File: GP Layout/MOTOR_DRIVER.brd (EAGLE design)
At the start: 91.4 x 97.5 mm, 34 parts, among them U2 CSD18502KCS_KCS_3, U3 MIC4604YM, U4 CSD18502KCS_KCS_3, U5 CSD18502KCS_KCS_3, U6 MIC4604YM, U7 ATMEGA328P_TQFP, Y1 16MHz

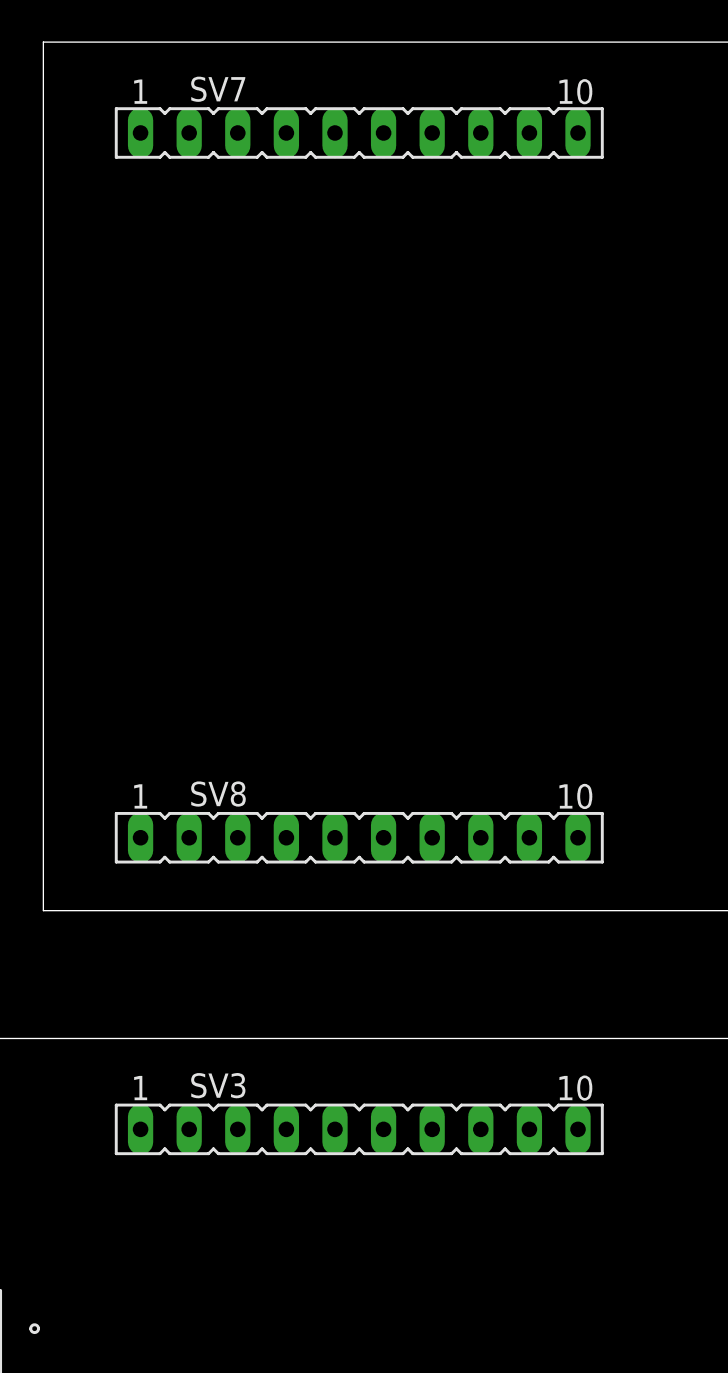
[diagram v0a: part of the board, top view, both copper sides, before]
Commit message: component placement
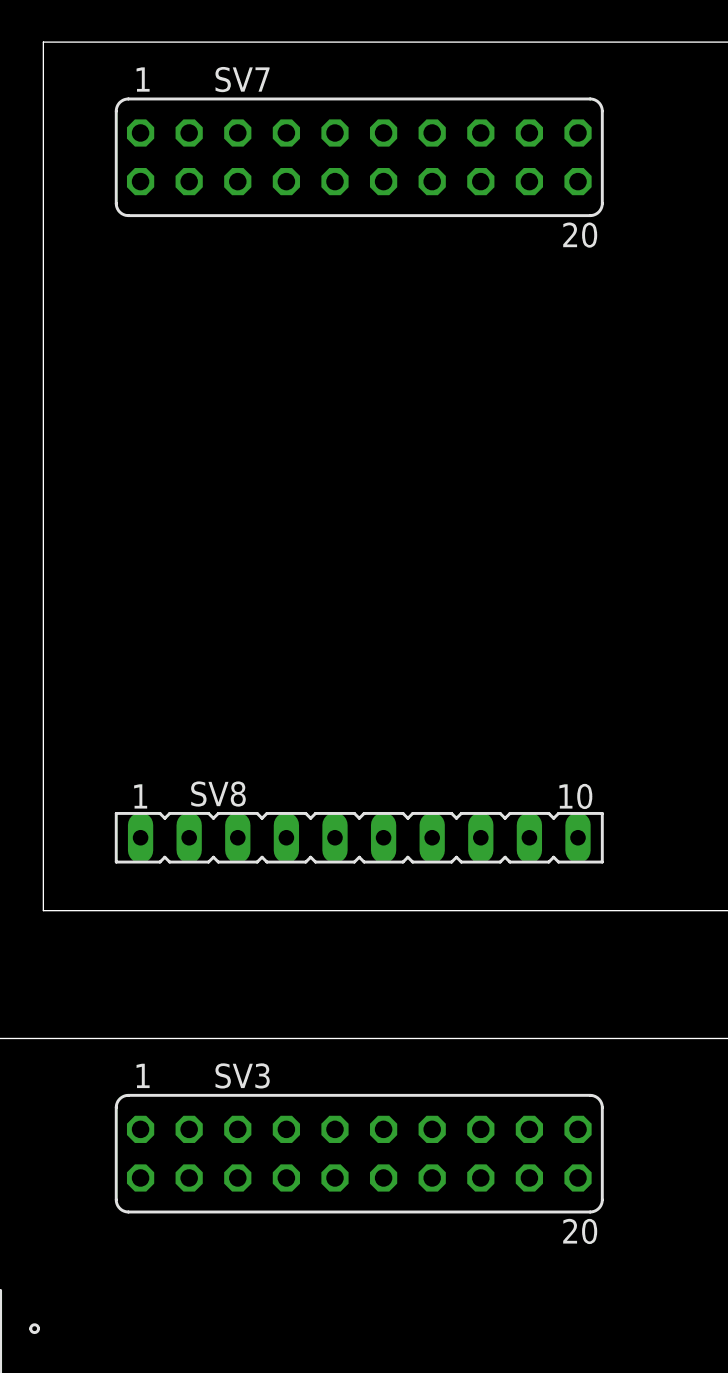
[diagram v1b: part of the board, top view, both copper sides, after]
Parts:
- SV3, SV7: device con-lsta:FE10 -> con-lsta:FE10-2
- moved SV3 1.27 mm to (69.8, 39.4)
- moved SV7 1.27 mm to (69.8, 91.4)
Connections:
- new net N$27: SV3.12
- net 3_3V: now also SV3.9
- net 5V: now also SV3.18, SV3.7
- net BLT_RX: now also SV3.1
- net BLT_TX: now also SV3.3
- net CAMERA_A0: now also SV3.17
- net CAMERA_CLK: now also SV3.13
- net CAMERA_SI: now also SV3.15
- net GND: now also SV3.11, SV3.14, SV3.5
- net HALL: now also SV3.16
- net RX: now also SV3.20
- net TX: now also SV3.19
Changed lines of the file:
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@@
 <attribute name="MF" value="" x="21.59" y="3.81" size="1.778" layer="27" display="off"/>
-</element>
-<element name="SV3" library="con-lsta" package="FE10" value="" x="69.85" y="40.64">
-<attribute name="OC_FARNELL" value="unknown" x="69.85" y="40.64" size="1.778" layer="27" display="off"/>
-<attribute name="MPN" value="" x="69.85" y="40.64" size="1.778" layer="27" display="off"/>
-<attribute name="OC_NEWARK" value="unknown" x="69.85" y="40.64" size="1.778" layer="27" display="off"/>
-<attribute name="MF" value="" x="69.85" y="40.64" size="1.778" layer="27" display="off"/>
 </element>
 <element name="SV4" library="con-lsta" package="FE10" value="" x="69.85" y="3.81">
@@
 <attribute name="MF" value="" x="21.59" y="55.88" size="1.778" layer="27" display="off"/>
 </element>
-<element name="SV7" library="con-lsta" package="FE10" value="" x="69.85" y="92.71">
-<attribute name="OC_FARNELL" value="unknown" x="69.85" y="92.71" size="1.778" layer="27" display="off"/>
-<attribute name="MPN" value="" x="69.85" y="92.71" size="1.778" layer="27" display="off"/>
-<attribute name="OC_NEWARK" value="unknown" x="69.85" y="92.71" size="1.778" layer="27" display="off"/>
-<attribute name="MF" value="" x="69.85" y="92.71" size="1.778" layer="27" display="off"/>
-</element>
 <element name="SV8" library="con-lsta" package="FE10" value="" x="69.85" y="55.88">
 <attribute name="OC_FARNELL" value="unknown" x="69.85" y="55.88" size="1.778" layer="27" display="off"/>
@@
 <attribute name="OC_NEWARK" value="unknown" x="69.85" y="55.88" size="1.778" layer="27" display="off"/>
 <attribute name="MF" value="" x="69.85" y="55.88" size="1.778" layer="27" display="off"/>
+</element>
+<element name="SV3" library="con-lsta" package="FE10-2" value="" x="69.85" y="39.37">
+<attribute name="OC_FARNELL" value="unknown" x="69.85" y="39.37" size="1.778" layer="27" display="off"/>
+<attribute name="MPN" value="" x="69.85" y="39.37" size="1.778" layer="27" display="off"/>
+<attribute name="OC_NEWARK" value="unknown" x="69.85" y="39.37" size="1.778" layer="27" display="off"/>
+<attribute name="MF" value="" x="69.85" y="39.37" size="1.778" layer="27" display="off"/>
+</element>
+<element name="SV7" library="con-lsta" package="FE10-2" value="" x="69.85" y="91.44">
+<attribute name="OC_FARNELL" value="unknown" x="69.85" y="91.44" size="1.778" layer="27" display="off"/>
+<attribute name="MPN" value="" x="69.85" y="91.44" size="1.778" layer="27" display="off"/>
+<attribute name="OC_NEWARK" value="unknown" x="69.85" y="91.44" size="1.778" layer="27" display="off"/>
+<attribute name="MF" value="" x="69.85" y="91.44" size="1.778" layer="27" display="off"/>
 </element>
 </elements>
@@
 <contactref element="S1" pad="12"/>
 <contactref element="SV1" pad="10"/>
-<wire x1="79.3242" y1="17.78" x2="79.3242" y2="20.32" width="0" layer="19" extent="1-1"/>
+<contactref element="SV3" pad="5"/>
+<contactref element="SV3" pad="11"/>
+<contactref element="SV3" pad="14"/>
+<wire x1="73.66" y1="38.1" x2="71.12" y2="40.64" width="0" layer="19" extent="1-1"/>
+<wire x1="63.5" y1="40.64" x2="71.12" y2="40.64" width="0" layer="19" extent="1-1"/>
+<wire x1="48.26" y1="34.29" x2="63.5" y2="40.64" width="0" layer="19" extent="1-1"/>
+<wire x1="48.26" y1="30.226" x2="48.26" y2="34.29" width="0" layer="19" extent="1-1"/>
+<wire x1="45.72" y1="24.13" x2="48.26" y2="30.226" width="0" layer="19" extent="1-1"/>
+<wire x1="53.34" y1="21.59" x2="45.72" y2="24.13" width="0" layer="19" extent="1-1"/>
+<wire x1="59.2074" y1="17.71" x2="53.34" y2="21.59" width="0" layer="19" extent="1-1"/>
+<wire x1="59.2074" y1="16.11" x2="59.2074" y2="17.71" width="0" layer="19" extent="1-1"/>
+<wire x1="67.7926" y1="16.91" x2="59.2074" y2="17.71" width="0" layer="19" extent="1-1"/>
+<wire x1="50.8" y1="11.43" x2="59.2074" y2="16.11" width="0" layer="19" extent="1-1"/>
+<wire x1="79.3242" y1="17.78" x2="67.7926" y2="16.91" width="0" layer="19" extent="1-1"/>
+<wire x1="79.3242" y1="20.32" x2="79.3242" y2="17.78" width="0" layer="19" extent="1-1"/>
 <wire x1="79.3242" y1="15.24" x2="79.3242" y2="17.78" width="0" layer="19" extent="1-1"/>
 <wire x1="79.3242" y1="12.7" x2="79.3242" y2="15.24" width="0" layer="19" extent="1-1"/>
 <wire x1="79.3242" y1="10.16" x2="79.3242" y2="12.7" width="0" layer="19" extent="1-1"/>
-<wire x1="67.7926" y1="16.91" x2="79.3242" y2="17.78" width="0" layer="19" extent="1-1"/>
-<wire x1="59.2074" y1="16.11" x2="67.7926" y2="16.91" width="0" layer="19" extent="1-1"/>
-<wire x1="59.2074" y1="17.71" x2="59.2074" y2="16.11" width="0" layer="19" extent="1-1"/>
-<wire x1="53.34" y1="21.59" x2="59.2074" y2="17.71" width="0" layer="19" extent="1-1"/>
-<wire x1="45.72" y1="24.13" x2="53.34" y2="21.59" width="0" layer="19" extent="1-1"/>
-<wire x1="48.26" y1="30.226" x2="45.72" y2="24.13" width="0" layer="19" extent="1-1"/>
-<wire x1="48.26" y1="34.29" x2="48.26" y2="30.226" width="0" layer="19" extent="1-1"/>
-<wire x1="50.8" y1="11.43" x2="59.2074" y2="16.11" width="0" layer="19" extent="1-1"/>
 <wire x1="33.02" y1="40.64" x2="48.26" y2="34.29" width="0" layer="19" extent="1-1"/>
 <wire x1="12.7" y1="24.13" x2="33.02" y2="40.64" width="0" layer="19" extent="1-1"/>
@@
 <signal name="HALL">
 <contactref element="U7" pad="32"/>
+<contactref element="SV3" pad="16"/>
+<wire x1="60.7" y1="20.8026" x2="76.2" y2="38.1" width="0" layer="19" extent="1-1"/>
 </signal>
 <signal name="CAMERA_CLK">
 <contactref element="U7" pad="12"/>
+<contactref element="SV3" pad="13"/>
+<wire x1="63.1" y1="12.2174" x2="73.66" y2="40.64" width="0" layer="19" extent="1-1"/>
 </signal>
 <signal name="CAMERA_SI">
 <contactref element="U7" pad="11"/>
+<contactref element="SV3" pad="15"/>
+<wire x1="62.3" y1="12.2174" x2="76.2" y2="40.64" width="0" layer="19" extent="1-1"/>
 </signal>
 <signal name="CAMERA_A0">
 <contactref element="U7" pad="23"/>
+<contactref element="SV3" pad="17"/>
+<wire x1="67.7926" y1="18.51" x2="78.74" y2="40.64" width="0" layer="19" extent="1-1"/>
 </signal>
 <signal name="SERVO">
@@
 <signal name="BLT_RX">
 <contactref element="U$1" pad="7"/>
+<contactref element="SV3" pad="1"/>
+<wire x1="30.48" y1="8.89" x2="58.42" y2="40.64" width="0" layer="19" extent="1-1"/>
 </signal>
 <signal name="BLT_TX">
 <contactref element="U$1" pad="8"/>
+<contactref element="SV3" pad="3"/>
+<wire x1="33.02" y1="8.89" x2="60.96" y2="40.64" width="0" layer="19" extent="1-1"/>
 </signal>
 <signal name="N$13">
@@
 <signal name="RX">
 <contactref element="U7" pad="30"/>
+<contactref element="SV3" pad="20"/>
+<wire x1="62.3" y1="20.8026" x2="81.28" y2="38.1" width="0" layer="19" extent="1-1"/>
 </signal>
 <signal name="TX">
 <contactref element="U7" pad="31"/>
+<contactref element="SV3" pad="19"/>
+<wire x1="61.5" y1="20.8026" x2="81.28" y2="40.64" width="0" layer="19" extent="1-1"/>
 </signal>
 <signal name="5V">
@@
 <contactref element="C7" pad="1"/>
 <contactref element="S1" pad="7"/>
+<contactref element="SV3" pad="7"/>
+<contactref element="SV3" pad="18"/>
+<wire x1="66.04" y1="40.64" x2="78.74" y2="38.1" width="0" layer="19" extent="1-1"/>
+<wire x1="79.3242" y1="22.86" x2="78.74" y2="38.1" width="0" layer="19" extent="1-1"/>
 <wire x1="67.7926" y1="14.51" x2="79.3242" y2="22.86" width="0" layer="19" extent="1-1"/>
 <wire x1="63.1" y1="20.8026" x2="67.7926" y2="14.51" width="0" layer="19" extent="1-1"/>
 <wire x1="59.2074" y1="16.91" x2="63.1" y2="20.8026" width="0" layer="19" extent="1-1"/>
 <wire x1="59.2074" y1="15.31" x2="59.2074" y2="16.91" width="0" layer="19" extent="1-1"/>
-<wire x1="43.18" y1="34.29" x2="59.2074" y2="16.91" width="0" layer="19" extent="1-1"/>
-<wire x1="45.72" y1="30.226" x2="43.18" y2="34.29" width="0" layer="19" extent="1-1"/>
+<wire x1="45.72" y1="30.226" x2="59.2074" y2="16.91" width="0" layer="19" extent="1-1"/>
+<wire x1="43.18" y1="34.29" x2="45.72" y2="30.226" width="0" layer="19" extent="1-1"/>
 </signal>
 <signal name="3_3V">
 <contactref element="U$1" pad="3V3_LO"/>
+<contactref element="SV3" pad="9"/>
+<wire x1="15.24" y1="24.13" x2="68.58" y2="40.64" width="0" layer="19" extent="1-1"/>
 </signal>
 <signal name="M1_GPIO1">
@@
 <wire x1="10.16" y1="40.64" x2="43.18" y2="30.226" width="0" layer="19" extent="1-1"/>
 </signal>
+<signal name="N$27">
+<contactref element="SV3" pad="12"/>
+</signal>
 </signals>
